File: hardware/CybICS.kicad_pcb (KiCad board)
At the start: 2 copper layers, 160 x 100 mm, 77 parts, among them J1 Raspberry_Pi_2_3, J2 Conn_01x03_Pin, J3 Conn_01x05_Pin, J4 USB_C_Receptacle_USB2.0, SW1 SW_Push, SW2 SW_Push, SW3 SW_Push, U1 STM32G070RBTx

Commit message: Hardware change for version 0.2
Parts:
- R1, R10, R2, R21, R23, R25, R4, R5, R6, R8: value 100R -> 330R

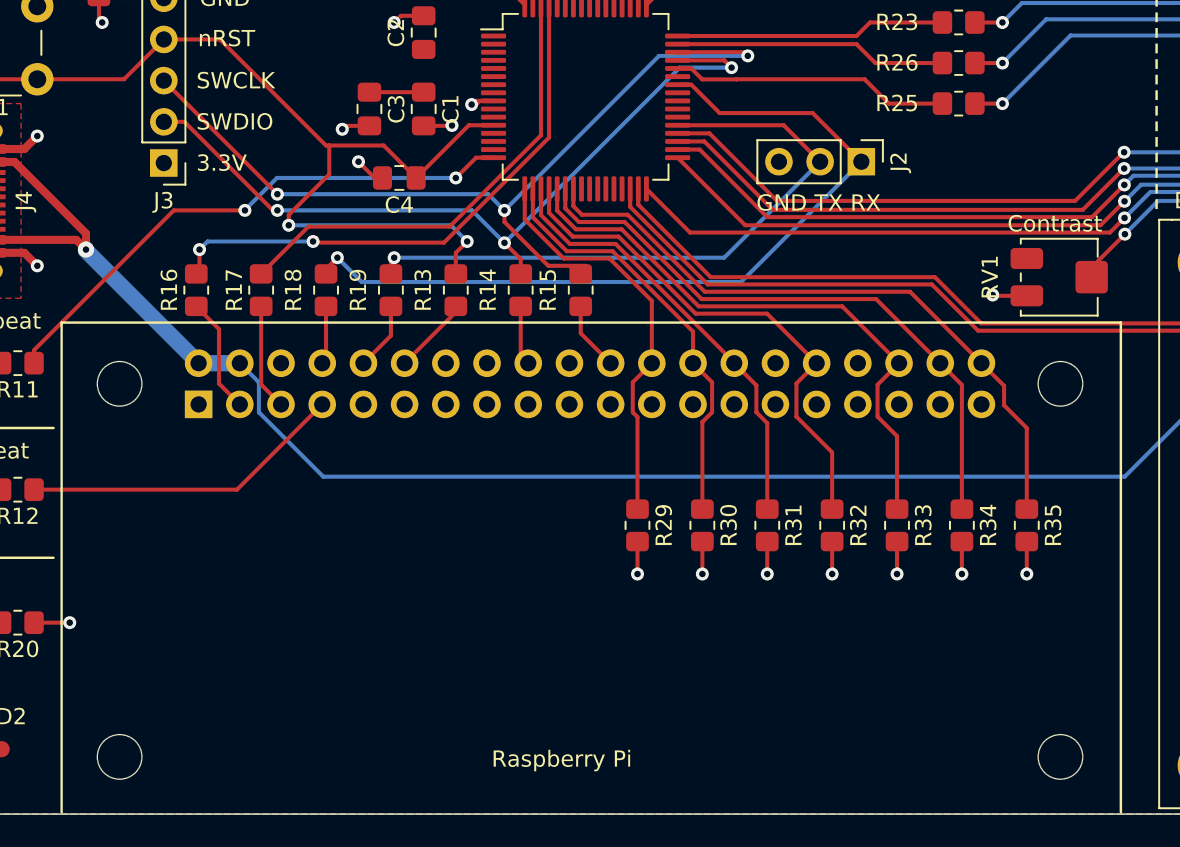
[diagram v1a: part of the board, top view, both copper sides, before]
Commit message: Changed J1 position to top
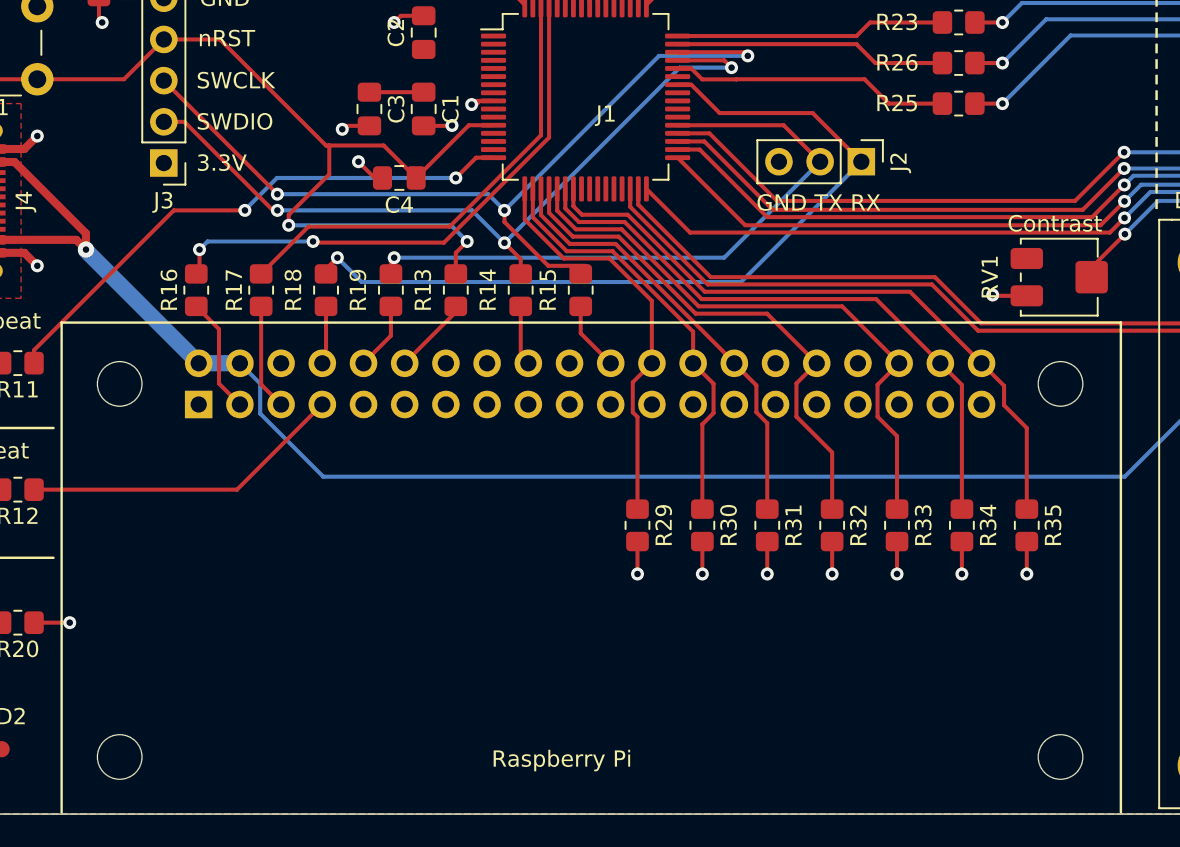
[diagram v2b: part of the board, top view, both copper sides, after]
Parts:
- J1: moved to F.Cu
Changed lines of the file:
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@@
     )
   )
-  (footprint "Module:Raspberry_Pi_Zero_Socketed_THT_FaceDown_MountingHoles" (layer "B.Cu")
-    (at 70.945 125.545 -90)
+  (footprint "Module:Raspberry_Pi_Zero_Socketed_THT_FaceDown_MountingHoles" (layer "F.Cu")
+    (at 70.95 125.55 -90)
     (descr "Raspberry Pi Zero using through hole straight pin socket, 2x20, 2.54mm pitch, https://www.raspberrypi.org/documentation/hardware/raspberrypi/mechanical/rpi_MECH_Zero_1p2.pdf")
     (tags "raspberry pi zero through hole")
@@
     (property "ki_keywords" "raspberrypi gpio")
     (attr through_hole)
-    (fp_text reference "J1" (at -17.901496 -25.13 180) (layer "B.SilkS")
-        (effects (font (size 1 1) (thickness 0.15)) (justify mirror))
-    )
-    (fp_text value "Raspberry_Pi_2_3" (at 10.23 -23.055 180) (layer "F.Fab")
+    (fp_text reference "J1" (at -17.901496 -25.13) (layer "F.SilkS")
         (effects (font (size 1 1) (thickness 0.15)))
     )
-    (fp_text user "${REFERENCE}" (at -1.27 -24.13 180) (layer "B.Fab")
-        (effects (font (size 1 1) (thickness 0.15)) (justify mirror))
+    (fp_text value "Raspberry_Pi_2_3" (at 10.23 -23.055) (layer "F.Fab")
+        (effects (font (size 1 1) (thickness 0.15)))
+    )
+    (fp_text user "${REFERENCE}" (at -1.27 -24.13) (layer "F.Fab")
+        (effects (font (size 1 1) (thickness 0.15)))
     )
     (fp_line (start -4.83 -53.63) (end -4.83 5.37)
@@
   (segment (start 64 116.06) (end 70.945 123.005) (width 1) (layer "B.Cu") (net 32))
   (segment (start 64 116) (end 64 116.06) (width 0.25) (layer "B.Cu") (net 32))
-  (segment (start 74.66 126.031701) (end 74.66 124.18) (width 0.25) (layer "B.Cu") (net 32))
+  (segment (start 74.74 126.111701) (end 74.74 124.26) (width 0.25) (layer "B.Cu") (net 32))
   (segment (start 128.03982 130) (end 78.628299 130) (width 0.25) (layer "B.Cu") (net 32))
+  (segment (start 140.84052 117.1993) (end 128.03982 130) (width 0.25) (layer "B.Cu") (net 32))
+  (segment (start 74.74 124.26) (end 73.485 123.005) (width 0.25) (layer "B.Cu") (net 32))
   (segment (start 73.485 123.005) (end 70.945 123.005) (width 1) (layer "B.Cu") (net 32))
-  (segment (start 74.66 124.18) (end 73.485 123.005) (width 0.25) (layer "B.Cu") (net 32))
-  (segment (start 78.628299 130) (end 74.66 126.031701) (width 0.25) (layer "B.Cu") (net 32))
+  (segment (start 78.628299 130) (end 74.74 126.111701) (width 0.25) (layer "B.Cu") (net 32))
   (segment (start 140.84052 116.7993) (end 140.84052 117.1993) (width 0.25) (layer "B.Cu") (net 32))
-  (segment (start 140.84052 117.1993) (end 128.03982 130) (width 0.25) (layer "B.Cu") (net 32))
   (segment (start 154.3125 85.8) (end 152.8 85.8) (width 0.25) (layer "F.Cu") (net 33))
   (segment (start 154.3125 85.8) (end 154.2875 85.8) (width 0.25) (layer "F.Cu") (net 33))
@@
   (segment (start 98.885 119.157792) (end 98.885 123.005) (width 0.25) (layer "F.Cu") (net 102))
   (segment (start 96.277208 116.55) (end 98.885 119.157792) (width 0.25) (layer "F.Cu") (net 102))
-  (segment (start 101.425 123.005) (end 101.425 121.061396) (width 0.25) (layer "F.Cu") (net 103))
-  (segment (start 101.425 121.061396) (end 96.463604 116.1) (width 0.25) (layer "F.Cu") (net 103))
-  (segment (start 102 132) (end 102 126.631701) (width 0.25) (layer "F.Cu") (net 103))
+  (segment (start 102 132) (end 102 126.77) (width 0.25) (layer "F.Cu") (net 103))
+  (segment (start 102 126.77) (end 102.69 126.08) (width 0.25) (layer "F.Cu") (net 103))
+  (segment (start 102.69 124.27) (end 101.43 123.01) (width 0.25) (layer "F.Cu") (net 103))
+  (segment (start 102.69 126.08) (end 102.69 124.27) (width 0.25) (layer "F.Cu") (net 103))
+  (segment (start 93.642012 116.1) (end 91.55 114.007988) (width 0.25) (layer "F.Cu") (net 103))
+  (segment (start 91.55 114.007988) (end 91.55 112.259252) (width 0.25) (layer "F.Cu") (net 103))
   (segment (start 96.463604 116.1) (end 93.642012 116.1) (width 0.25) (layer "F.Cu") (net 103))
-  (segment (start 91.55 114.007988) (end 91.55 112.259252) (width 0.25) (layer "F.Cu") (net 103))
-  (segment (start 93.642012 116.1) (end 91.55 114.007988) (width 0.25) (layer "F.Cu") (net 103))
-  (segment (start 102 126.631701) (end 102.6 126.031701) (width 0.25) (layer "F.Cu") (net 103))
-  (segment (start 102.6 124.18) (end 101.425 123.005) (width 0.25) (layer "F.Cu") (net 103))
-  (segment (start 102.6 126.031701) (end 102.6 124.18) (width 0.25) (layer "F.Cu") (net 103))
+  (segment (start 101.43 123.01) (end 101.43 121.066396) (width 0.25) (layer "F.Cu") (net 103))
+  (segment (start 101.43 121.066396) (end 96.463604 116.1) (width 0.25) (layer "F.Cu") (net 103))
   (segment (start 105.33 124.37) (end 103.965 123.005) (width 0.25) (layer "F.Cu") (net 104))
   (segment (start 106 126.701701) (end 105.33 126.031701) (width 0.25) (layer "F.Cu") (net 104))

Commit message: Fixing error with REF**
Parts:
- renumbered REF** to #SYM1
